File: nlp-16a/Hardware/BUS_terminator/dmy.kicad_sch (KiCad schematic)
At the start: 22 parts, among them J8 Conn_02x10_Odd_Even, J9 Conn_02x10_Odd_Even, U13 CD74HC00, U14 CD74HC00, U15 CD74HC00, U16 CD74HC00, U17 CD74HC00, U18 CD74HC00, U19 CD74HC00, U20 CD74HC00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

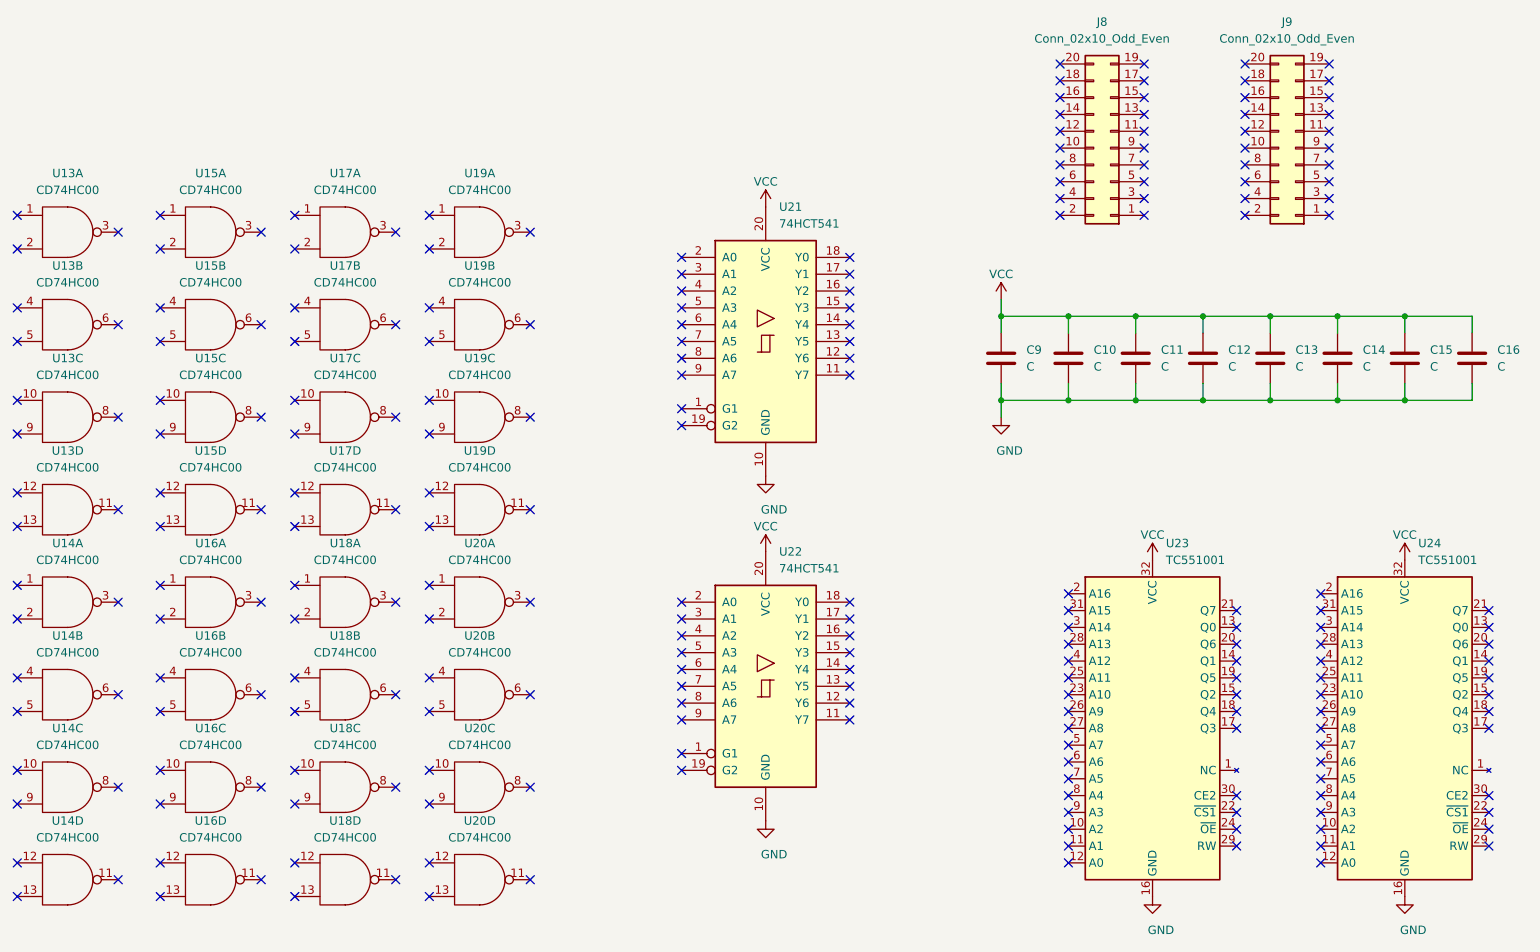
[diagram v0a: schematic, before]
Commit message: v1.1全ガーバーを更新
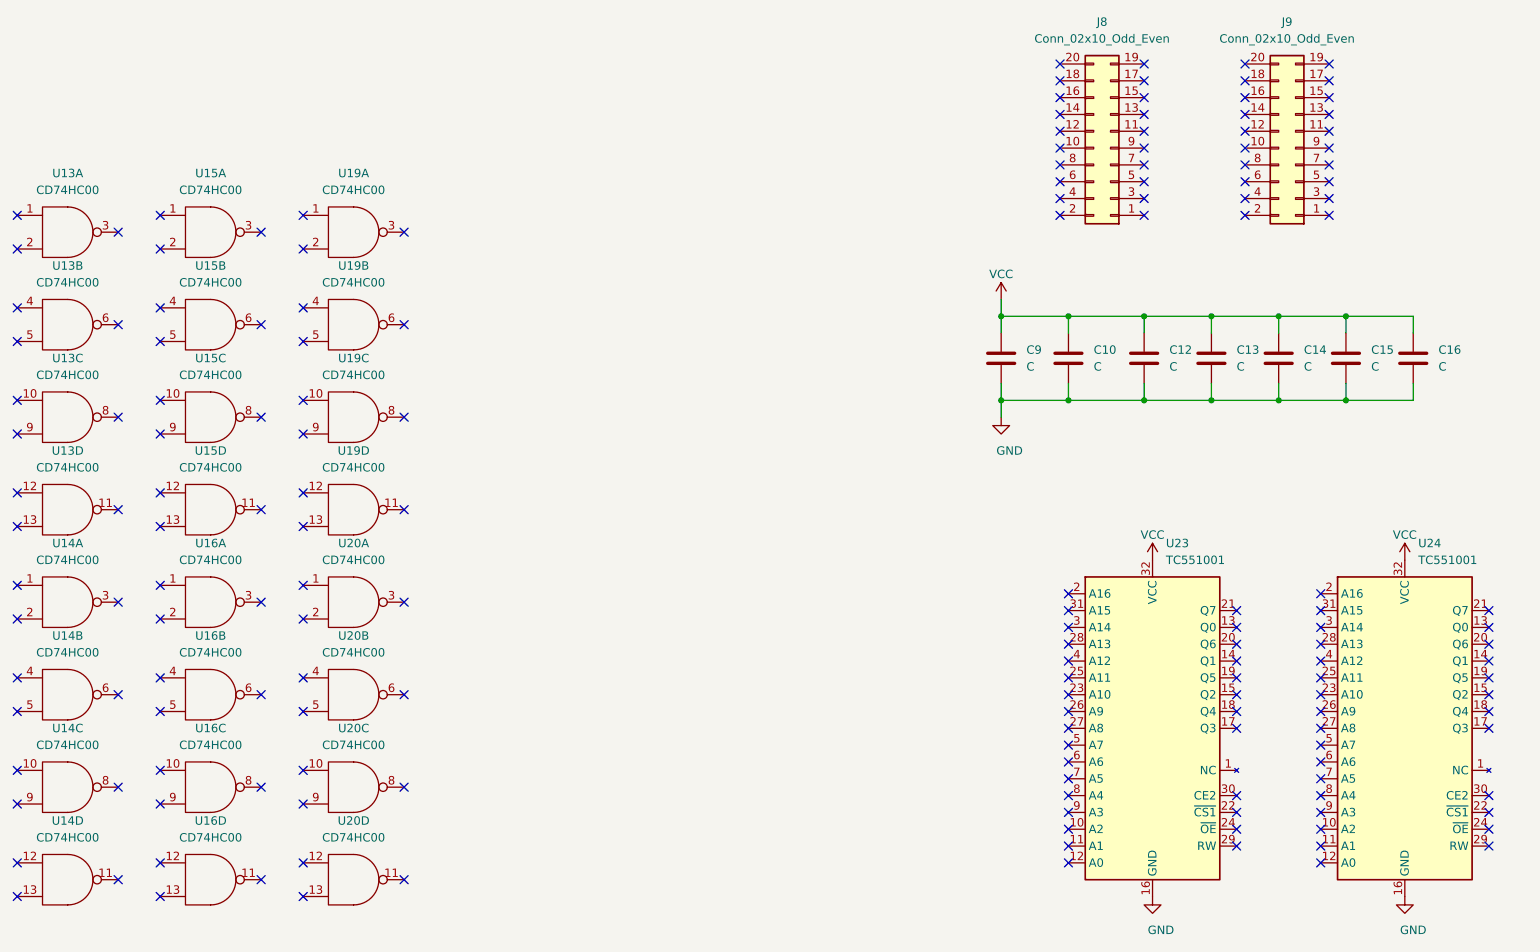
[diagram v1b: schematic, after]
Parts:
- removed C11: C, Capacitor_THT:C_Disc_D7.5mm_W2.5mm_P5.00mm, symbol Device:C
- removed U17, U18: CD74HC00, Package_DIP:DIP-14_W7.62mm, symbol CD74HCXX:CD74HC00
- removed U21, U22: 74HCT541, Package_DIP:DIP-20_W7.62mm, symbol 74xx:74HCT541
- C10, C12, C13, C14, C15, C16, C9: footprint Capacitor_THT:C_Disc_D7.5mm_W2.5mm_P5.00mm -> Capacitor_THT:C_Disc_D7.0mm_W2.5mm_P5.00mm
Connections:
- no-connect marks 230 -> 170
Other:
- moved on the sheet: C12, C13, C14, C15, C16, U19A, U19B, U19C, U19D, U20A, U20B, U20C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
